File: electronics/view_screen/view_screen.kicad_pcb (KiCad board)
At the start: 2 copper layers, 35 x 35 mm, 10 parts, among them J1 Conn_01x04, J2 GC9A01, J3 Conn_01x04, Q1 2N7002

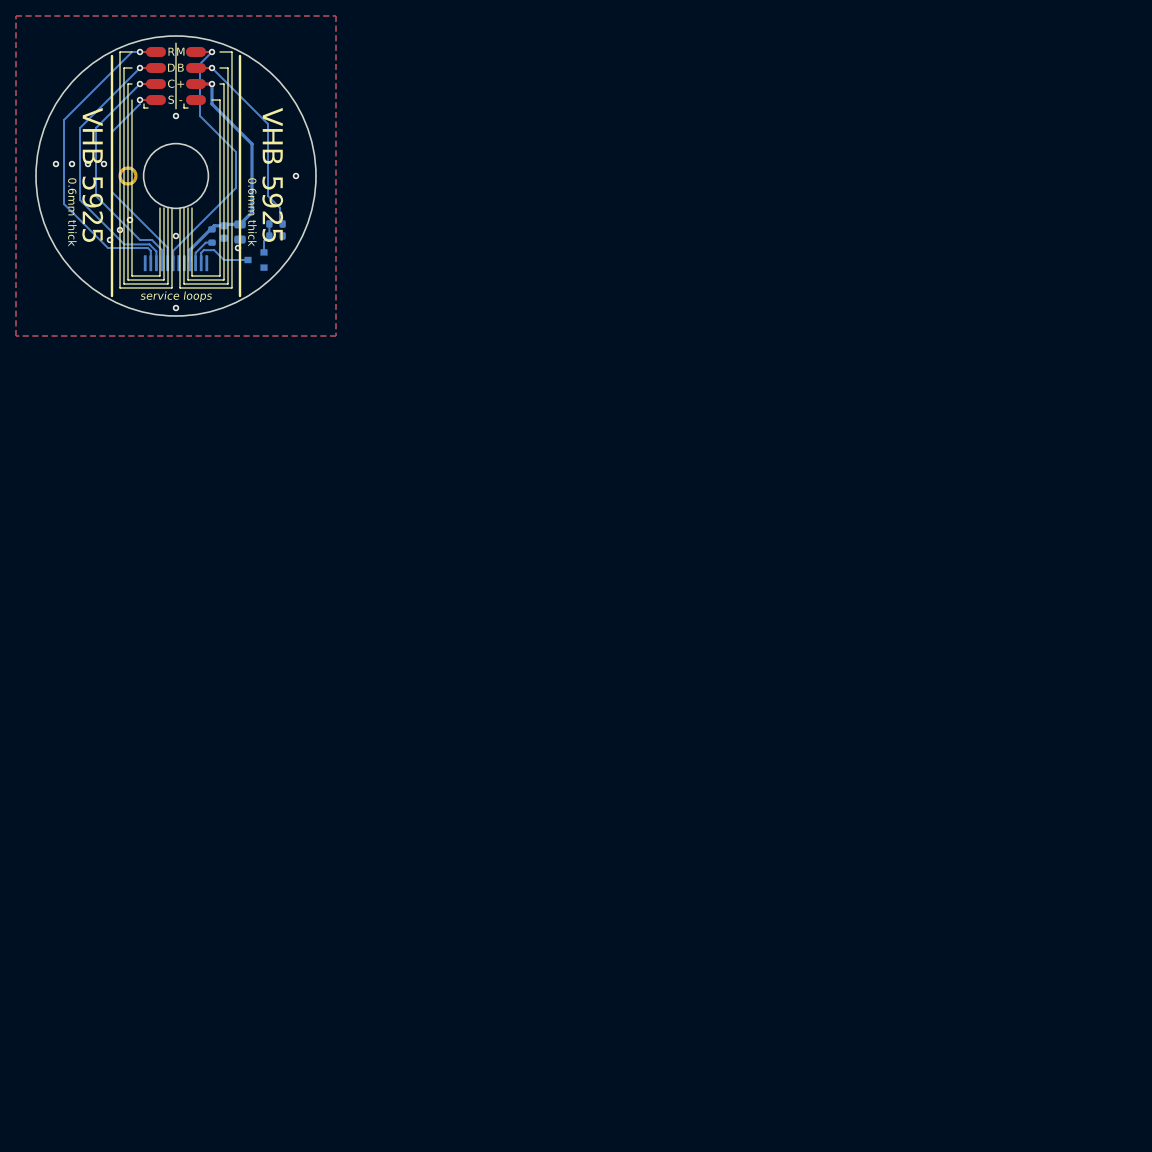
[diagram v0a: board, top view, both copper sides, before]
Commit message: Fab automation (#2)
- Use KiKit for fab automation
- Add splitflap scripts for exporting pcb pdfs, and switch to splitflap script for 3d rendering (for consistency with fab automation)
- Added support in 3d rendering scripts for soldermask & silkscreen colors, option to skip virtual components
- Added silkscreen to base and screen pcbs for commit and date info
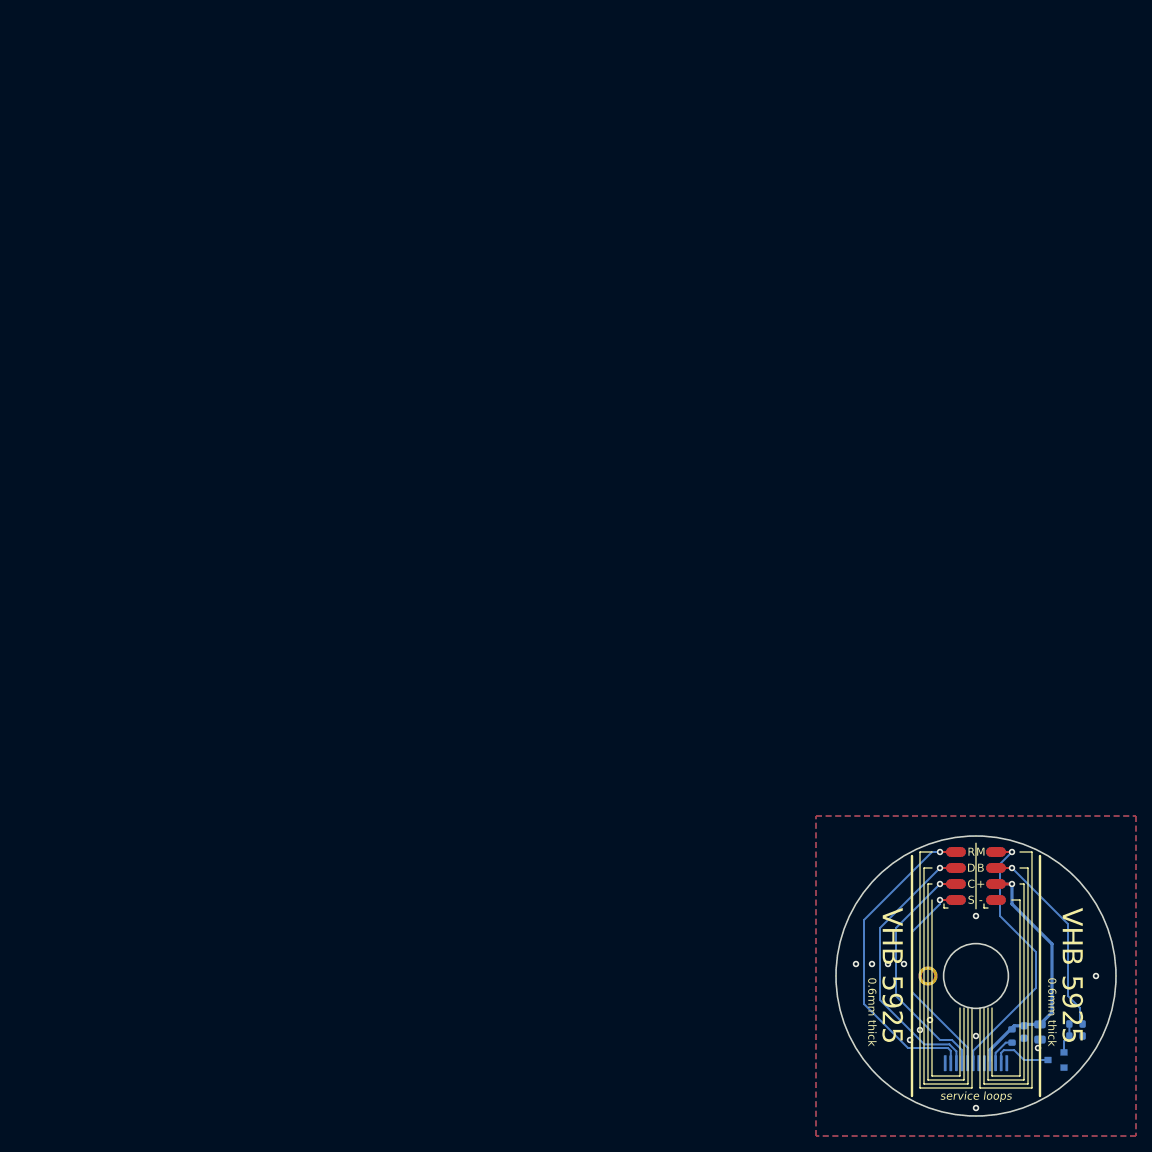
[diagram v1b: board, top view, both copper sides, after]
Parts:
- moved C1 141.4 mm to (108.0, 107.0)
- moved C2 141.4 mm to (106.0, 107.0)
- moved H1 141.4 mm to (94.0, 100.0)
- moved J1 141.4 mm to (102.5, 90.5)
- moved J2 141.4 mm to (100.0, 110.9)
- moved J3 141.4 mm to (97.5, 90.5)
- moved Q1 141.4 mm to (110.0, 110.5)
- moved R1 141.4 mm to (112.5, 106.0)
- moved R2 141.4 mm to (104.5, 107.5)
- moved R3 141.4 mm to (112.5, 107.5)
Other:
- outline, holes or cut-outs redrawn
- board text added: "DATE: YYYY-MM-DD COMMIT: deadbeef"
- board text added: "Screen PCB v0.1"
- board text added: "SmartKnob View"

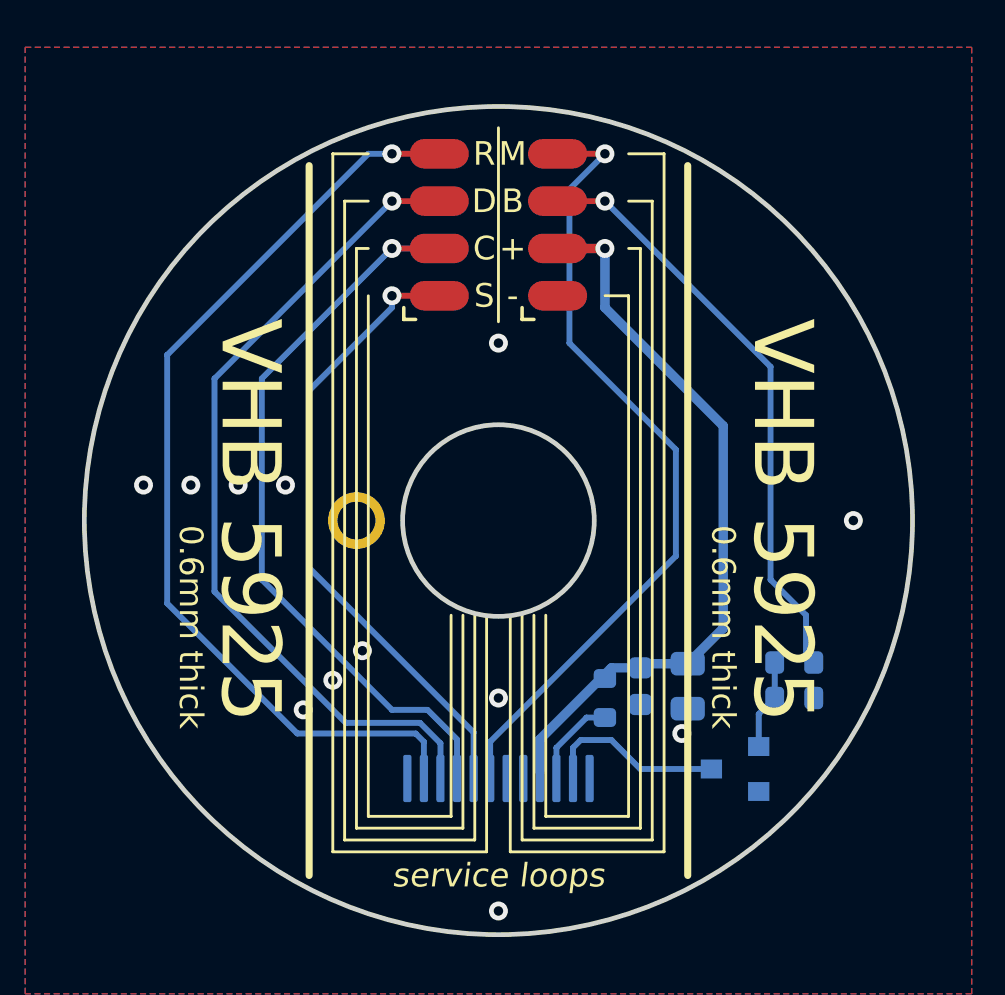
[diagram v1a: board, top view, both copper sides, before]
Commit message: View screen pcb: move solderpads to bottom to avoid shorting on metal LCD shield
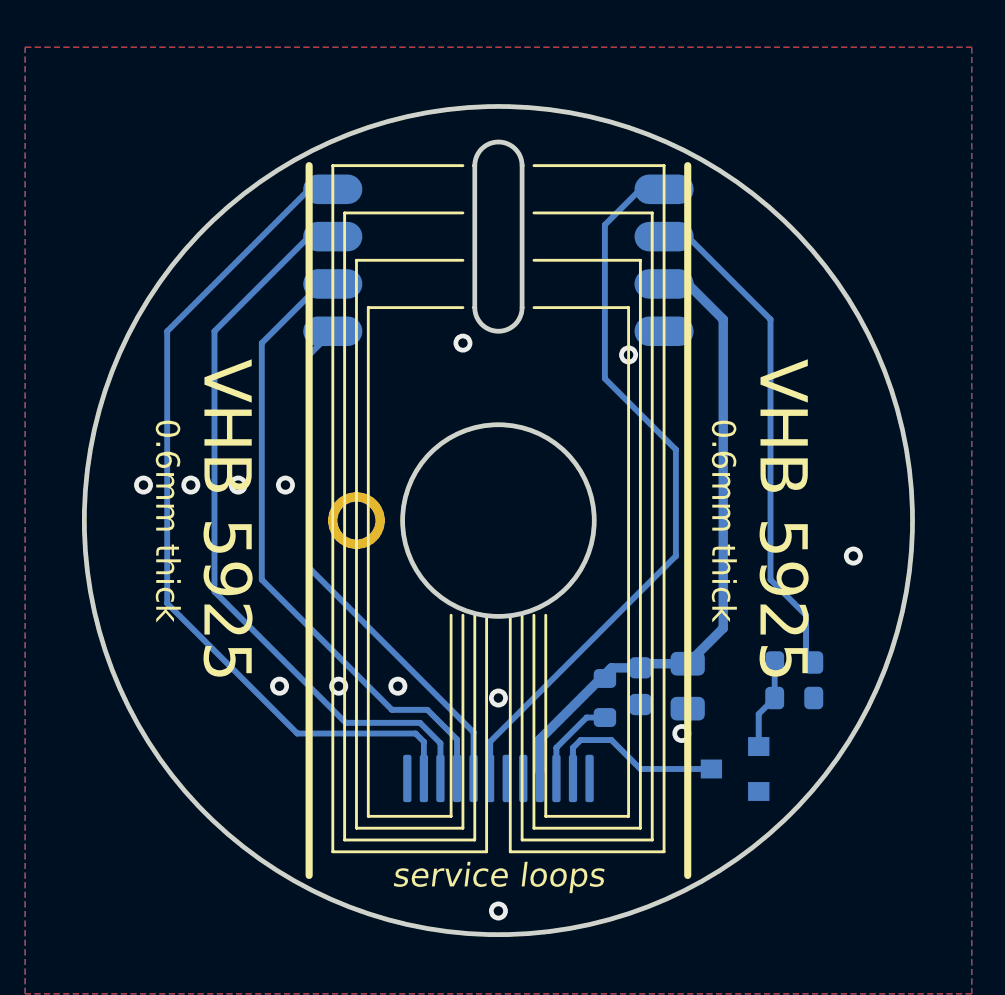
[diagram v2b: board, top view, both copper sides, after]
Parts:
- J1, J3: moved to B.Cu
- moved J1 4.74 mm to (107.0, 92.0)
- moved J3 4.74 mm to (93.0, 92.0)
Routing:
- net /nRESET: track 40.0 -> 35.5 mm, vias 1 -> 0
- net /nCS: track 26.4 -> 21.9 mm, vias 1 -> 0
- net /SCK: track 30.7 -> 26.4 mm, vias 1 -> 0
- net /VDD: track 31.2 -> 27.2 mm, vias 1 -> 0
- net /MOSI: track 35.0 -> 31.0 mm, vias 1 -> 0
- net /BACKLIGHT_EN: track 25.2 -> 21.2 mm, vias 1 -> 0
- net /DC: track 33.8 -> 30.7 mm, vias 1 -> 0
- net GND: vias 12 -> 13
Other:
- outline, holes or cut-outs redrawn
- board text added: "COMMIT: deadbeef DATE: YYYY-MM-DD"
- board text removed: "DATE: YYYY-MM-DD COMMIT: deadbeef"

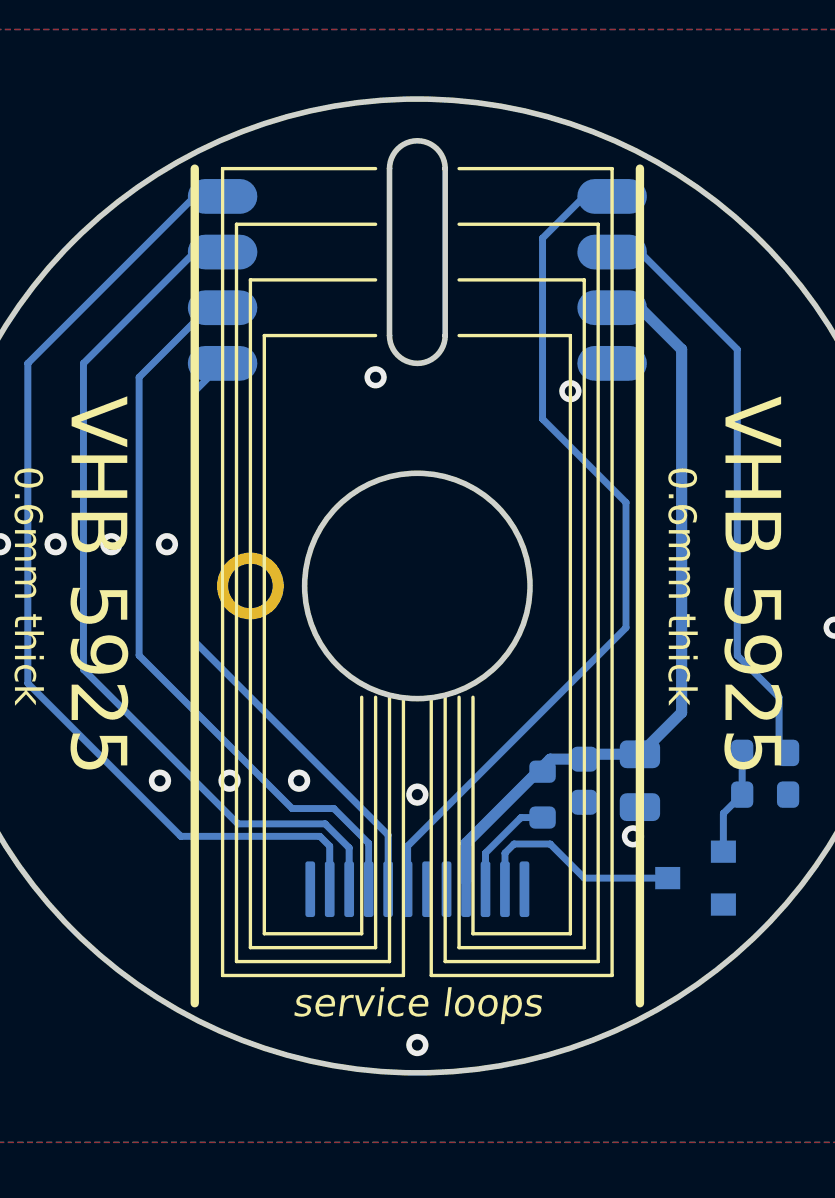
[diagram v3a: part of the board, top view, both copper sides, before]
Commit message: Remove "service loop" silkscreen marks from screen pcb
Service loops weren't really feasible/helpful, so don't recommend them via the silkscreen. Fixes #10

Also added testpoints (or could be solder points) for all signals on the top side of the screen PCB. Fixes #11
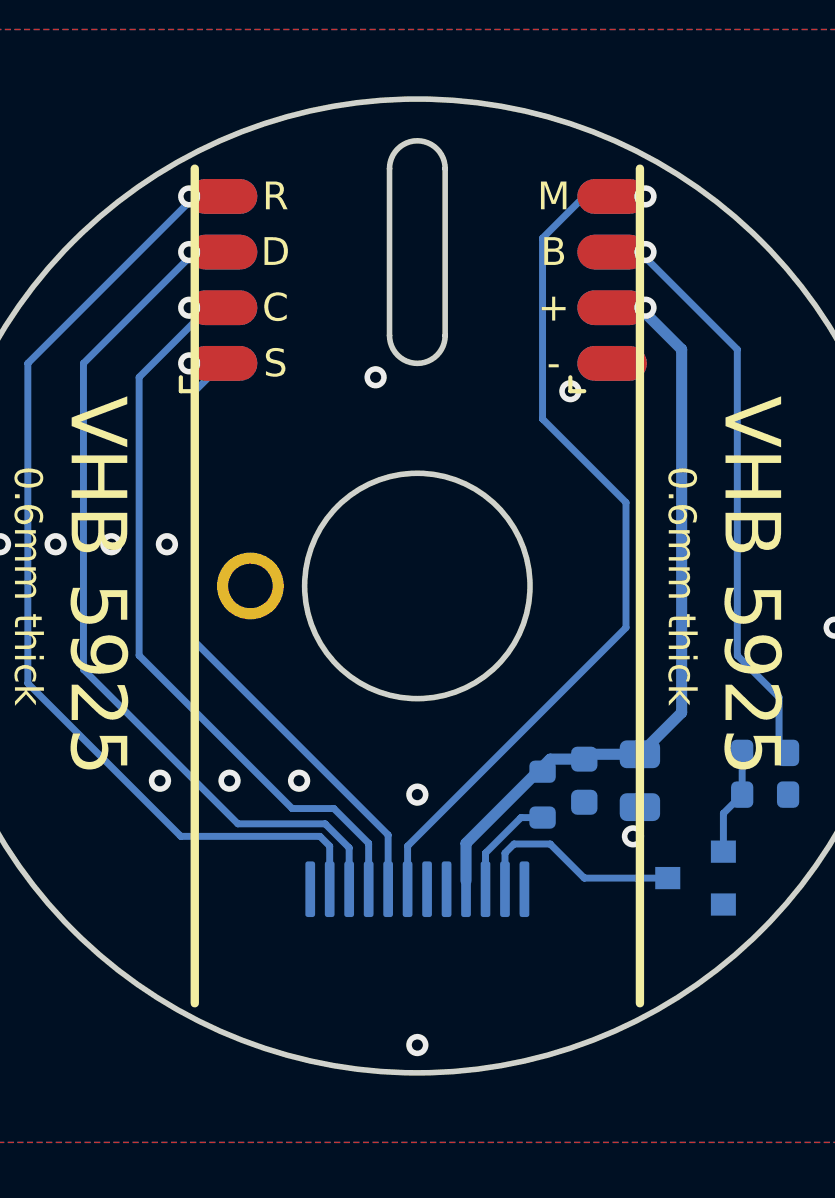
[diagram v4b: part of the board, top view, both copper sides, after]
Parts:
- added J4: Conn_01x04, SolderPads:SolderPads_2mm_4, F.Cu at (107.0, 92.0)
- added J5: Conn_01x04, SolderPads:SolderPads_2mm_4, F.Cu at (93.0, 92.0)
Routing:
- net /DC: vias 0 -> 1
- net /nRESET: vias 0 -> 1
- net /nCS: vias 0 -> 1
- net /VDD: vias 0 -> 1
- net /SCK: vias 0 -> 1
- net /MOSI: vias 0 -> 1
- net /BACKLIGHT_EN: vias 0 -> 1
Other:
- board text added: "SmartKnob"
- board text added: "View"
- board text removed: "SmartKnob View"
- board text removed: "service loops"
